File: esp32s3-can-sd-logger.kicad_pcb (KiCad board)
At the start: 4 copper layers, 84 x 100 mm, 194 parts, among them J1 PWR + CAN harness, J10 Sensor harness, J2 USB-C, J3 UART0, J4 I2C / Qwiic, J5 SPI, J6 WS2812, J7 Spare IO, J8 Rail break-out, J9 microSD push-pull, Q1 100V 6.8mOhm N-ch, Q2 P-ch 30V 3A, Q3 N-ch 60V 200mA, Q4 -20V 2.3A P-ch, Q5 60V 300mA N-ch, SW1 RESET, SW2 BOOT, U1 LM74700-Q1, U2 TLV431A, U3 LM5164 (5V), U4 LM5164 (3V3), U5 ESP32-S3-WROOM-1-N16R8, U6 USBLC6-2SC6, U7 74AHCT1G125, U8 TJA1051T/3, U9 ADS1115

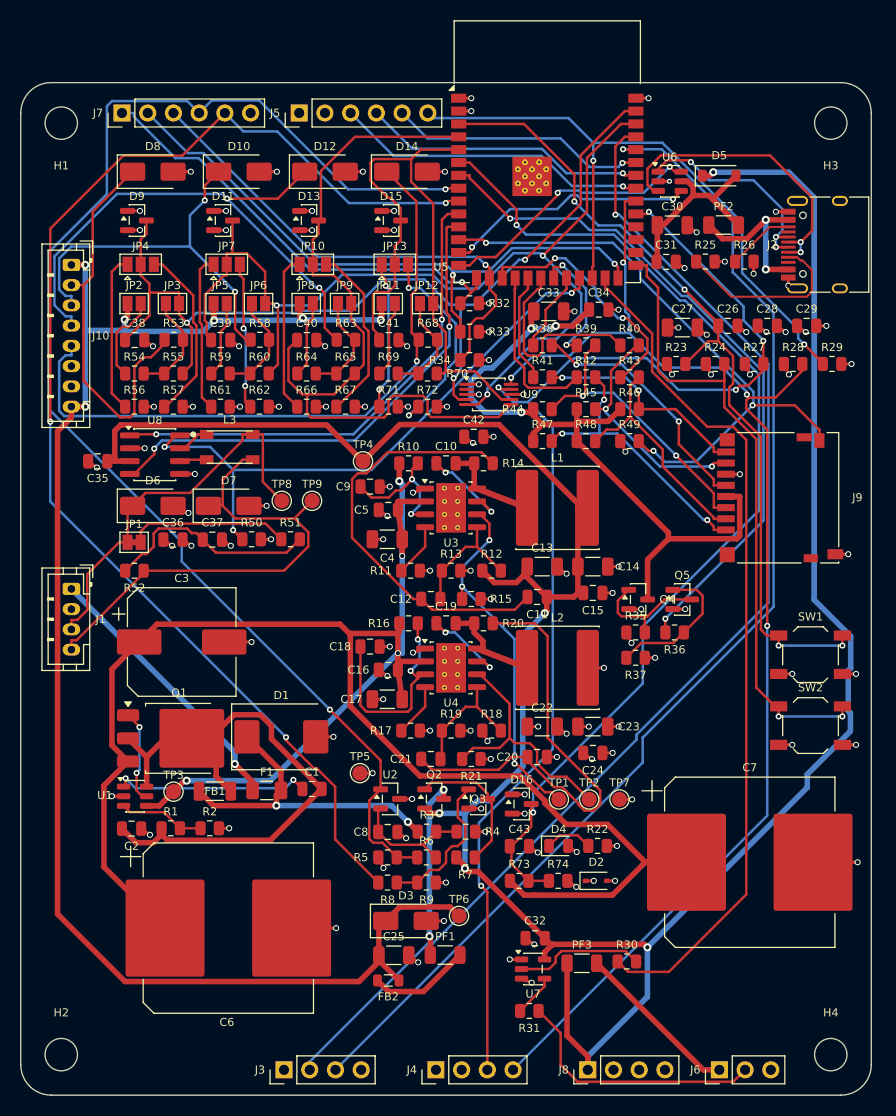
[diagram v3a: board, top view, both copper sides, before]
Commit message: USB OVP, card-slot ESD, SD test points, and a gold-standard schematic
Hardware, all simulation- or review-driven:
- USB overvoltage cutoff: TLV431 + AO3401 + MMBT3906 series switch on
  VBUS, tripping at 5.77 V. Re-simulated: a compliant 5 V source passes
  at 4.99 V, the switch opens at 5.95 V of brick, and the +5V rail never
  exceeds 5.2 V from anything up to 14 V -- where a 9 V brick previously
  drove it to 8.4 V against the TJA1051's 6 V absolute maximum.
  Off-the-shelf OVP parts were rejected first: the TPS25200 class cuts
  off near 7 V, which is no protection for a 6 V limit.
- Two SRV05-4 arrays clamp every microSD card contact (LCSC C13612);
  until now the ESP32's ~2 kV pin diodes were all that stood behind a
  card swapped by hand after every session.
- A second USBLC6 clamps the USB-C CC pins -- the first contacts every
  plug insertion touches, previously landing on bare 5.1k resistors.
- Test points on SD_CLK and SD_CMD, the most likely scope targets at
  bring-up and otherwise reachable only on fine-pitch pads.

The schematic itself was rebuilt to read like a reference design
(RejsaCAN was the benchmark): every circuit is now a hand-drawn block --
power-fail detector, sensor-rail switch, USB OVP, connector pull-
resistor clusters, and a single utility panel for test points, ERC
flags, mounting holes and the power LED. Sentence-length values became
part numbers ("0.2A PTC", "AO3401A", "600R") with ratings kept in
hidden fields, which also answers the external review's value-hygiene
findings. Title blocks carry rev B and a date. The Power sheet shrank
from A2 back to A3 in the process.

gen/README.md now documents the whole pipeline -- stages, the block-
drawing conventions with per-rotation pin geometry, the junction rules,
and the traps (property newlines, off-grid points, anchors keeping
their natural rotation) -- so the next board reuses all of it.

Board: 84 x 100, 0 DRC violations, 0 unconnected, 0 courtyard overlaps,
physical audit clean. BOM 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
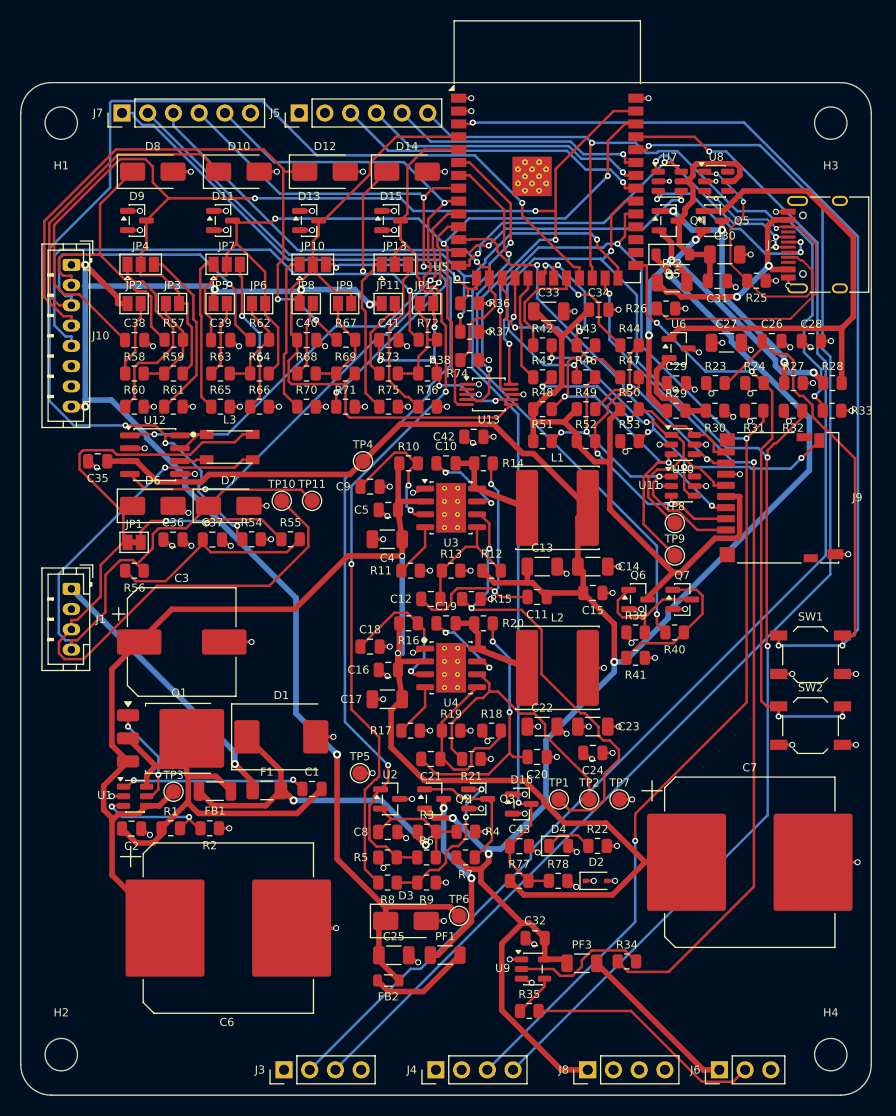
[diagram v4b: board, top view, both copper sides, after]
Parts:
- added Q6: DMG2301L, SOT-23, F.Cu at (61.0, 51.0)
- added Q7: 2N7002, SOT-23, F.Cu at (65.3, 51.0)
- added R75: 15k, R_0805_2012Metric, F.Cu at (36.3, 32.0)
- added R76: 2.21k, R_0805_2012Metric, F.Cu at (40.2, 32.0)
- added R77: 100k, R_0805_2012Metric, F.Cu at (49.2, 78.8)
- added R78: 8.2k, R_0805_2012Metric, F.Cu at (53.1, 78.8)
- added TP10: CAN_H, TestPoint_Pad_D1.5mm, F.Cu at (25.8, 41.3)
- added TP11: CAN_L, TestPoint_Pad_D1.5mm, F.Cu at (28.8, 41.3)
- added U10: SRV05-4, SOT-23-6, F.Cu at (65.4, 35.7)
- added U11: SRV05-4, SOT-23-6, F.Cu at (65.4, 39.8)
- added U12: TJA1051T/3, SOIC-8_3.9x4.9mm_P1.27mm, F.Cu at (13.2, 36.7)
- added U13: ADS1115, VSSOP-10_3x3mm_P0.5mm, F.Cu at (46.2, 30.8)
- FB1: value 600R @ 100MHz 3A -> 600R
- FB2: value 600R @ 100MHz 2A -> 600R
- L1: value 33uH 3A -> 33uH
- L2: value 22uH 3A -> 22uH
- L3: value 51uH CMC -> 51uH
- PF1: value 0.2A hold / 0.4A trip -> 0.2A PTC
- Q1: value 100V 6.8mOhm N-ch -> IPD068N10
- Q2: value P-ch 30V 3A -> AO3401A
- Q3: value N-ch 60V 200mA -> 2N7002
- Q4: value -20V 2.3A P-ch -> AO3401A
- Q5: value 60V 300mA N-ch -> MMBT3906
- R27: value 4.7k -> 100k
- R28: value 4.7k -> 10k
- R29: value 10k -> 100k
- R30: value 33 -> 27.4k
- R31: value 100 -> 4.7k
- R32: value 10k -> 4.7k
- R34, R44, R45, R46, R47: value 10k -> 33
- R35: value 100k -> 100
- R36: value 1k -> 10k
- R37: value 100k -> 10k
- R38: value 33 -> 10k
- R39, R41: value 33 -> 100k
- R40: value 33 -> 1k
- R49: value 47k -> 10k
- R51, R52: value 60.4 -> 10k
- R53: value 1k -> 47k
- R54, R59, R64, R69: value 2.49k -> 10k
- R55: value 10k -> 60.4
- R56: value 15k -> 60.4
- R57, R62, R67, R72: value 2.21k -> 1k
- R58, R63, R68: value 1k -> 2.49k
- R60, R65, R70: value 10k -> 15k
- R61, R66, R71: value 15k -> 2.21k
- R73: value 100k -> 2.49k
- R74: value 8.2k -> 10k
- TP8: value CAN_H -> SD_CLK
- TP9: value CAN_L -> SD_CMD
- U6: value USBLC6-2SC6 -> TLV431A; footprint SOT-23-6 -> SOT-23
- U7: value 74AHCT1G125 -> USBLC6-2SC6; footprint SOT-23-5 -> SOT-23-6
- U8: value TJA1051T/3 -> USBLC6-2SC6; footprint SOIC-8_3.9x4.9mm_P1.27mm -> SOT-23-6
- U9: value ADS1115 -> 74AHCT1G125; footprint VSSOP-10_3x3mm_P0.5mm -> SOT-23-5
- moved U7 79.0 mm to (64.1, 9.74)
- moved R31 63.3 mm to (72.4, 32.4)
- moved U8 61.7 mm to (68.7, 9.74)
- moved R34 61.4 mm to (59.9, 86.8)
- moved U9 56.9 mm to (50.6, 87.5)
- moved R30 55.1 mm to (68.6, 32.4)
- moved R73 51.7 mm to (36.3, 28.7)
- moved R74 51.7 mm to (40.2, 28.7)
- moved R52 46.4 mm to (55.8, 35.4)
- moved R53 46.1 mm to (60.1, 35.4)
- moved R50 39.5 mm to (60.1, 32.3)
- moved TP8 38.9 mm to (64.6, 43.5)
- moved R35 38.8 mm to (50.2, 91.7)
- moved R36 38.3 mm to (44.3, 21.8)
- moved Q4 37.5 mm to (64.0, 13.6)
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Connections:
- PF2 pad 2: VBUS -> VBUS_R
- Q4 pad 1: SD_PG -> VBUS_G
- Q4 pad 2: +3V3 -> VBUS_R
- Q4 pad 3: SD_VDD -> VBUS
- Q5 pad 1: SD_EN_G -> VBUS_OV
- Q5 pad 2: GND -> VBUS_R
- Q5 pad 3: SD_PG -> VBUS_G
- R27 pad 1: +3V3 -> VBUS_G
- R27 pad 2: I2C_SDA -> GND
- R28 pad 1: +3V3 -> VBUS_R
- R28 pad 2: I2C_SCL -> VBUS_OV
- R29 pad 1: SPI_CS -> VBUS_R
- R29 pad 2: +3V3 -> VBUS_OVS
- R30 pad 1: LED_DIN_MCU -> VBUS_OVS
- R30 pad 2: LED_DIN_A -> GND
- R31 pad 1: LED_DIN -> +3V3
- R31 pad 2: LED_DIN_J -> I2C_SDA
- R32 pad 1: IO3 -> +3V3
- R32 pad 2: GND -> I2C_SCL
- R33 pad 1: IO45 -> SPI_CS
- R33 pad 2: GND -> +3V3
- R34 pad 1: IO46 -> LED_DIN_MCU
- R34 pad 2: GND -> LED_DIN_A
- R35 pad 1: +3V3 -> LED_DIN
- R35 pad 2: SD_PG -> LED_DIN_J
- R36 pad 1: SD_PWR_EN -> IO3
- R36 pad 2: SD_EN_G -> GND
- R37 pad 1: SD_EN_G -> IO45
- R38 pad 1: SD_CLK -> IO46
- R38 pad 2: SD_CLK_C -> GND
- R39 pad 1: SD_CMD -> +3V3
- R39 pad 2: SD_CMD_C -> SD_PG
- R40 pad 1: SD_D0 -> SD_PWR_EN
- R40 pad 2: SD_D0_C -> SD_EN_G
- R41 pad 1: SD_D1 -> SD_EN_G
- R41 pad 2: SD_D1_C -> GND
- R42 pad 1: SD_D2 -> SD_CLK
- R42 pad 2: SD_D2_C -> SD_CLK_C
- R43 pad 1: SD_D3 -> SD_CMD
- R43 pad 2: SD_D3_C -> SD_CMD_C
- R44 pad 1: SD_VDD -> SD_D0
- R44 pad 2: SD_CMD_C -> SD_D0_C
- R45 pad 1: SD_VDD -> SD_D1
- R45 pad 2: SD_D0_C -> SD_D1_C
- R46 pad 1: SD_VDD -> SD_D2
- R46 pad 2: SD_D1_C -> SD_D2_C
- R47 pad 1: SD_VDD -> SD_D3
- R47 pad 2: SD_D2_C -> SD_D3_C
- R48 pad 2: SD_D3_C -> SD_CMD_C
- R49 pad 1: +3V3 -> SD_VDD
- R49 pad 2: SD_CD -> SD_D0_C
- R50 pad 1: CAN_S -> SD_VDD
- R50 pad 2: GND -> SD_D1_C
- R51 pad 1: TERM_A -> SD_VDD
- R51 pad 2: CAN_SPLIT -> SD_D2_C
- R52 pad 1: CAN_SPLIT -> SD_VDD
- R52 pad 2: CAN_L -> SD_D3_C
- R53 pad 1: AIN1_IN -> +3V3
- R53 pad 2: AIN1_A -> SD_CD
- R54 pad 1: AIN1_PU -> CAN_S
- R54 pad 2: AIN1_A -> GND
- R55 pad 1: AIN1_A -> TERM_A
- R55 pad 2: AIN1 -> CAN_SPLIT
- R56 pad 1: AIN1_R1 -> CAN_SPLIT
- R56 pad 2: GND -> CAN_L
- R57 pad 1: AIN1_R2 -> AIN1_IN
- R57 pad 2: GND -> AIN1_A
- R58 pad 1: AIN2_IN -> AIN1_PU
- R58 pad 2: AIN2_A -> AIN1_A
- R59 pad 1: AIN2_PU -> AIN1_A
- R59 pad 2: AIN2_A -> AIN1
- R60 pad 1: AIN2_A -> AIN1_R1
- R60 pad 2: AIN2 -> GND
- R61 pad 1: AIN2_R1 -> AIN1_R2
- R62 pad 1: AIN2_R2 -> AIN2_IN
- R62 pad 2: GND -> AIN2_A
- R63 pad 1: AIN3_IN -> AIN2_PU
- R63 pad 2: AIN3_A -> AIN2_A
- R64 pad 1: AIN3_PU -> AIN2_A
- R64 pad 2: AIN3_A -> AIN2
- R65 pad 1: AIN3_A -> AIN2_R1
- R65 pad 2: AIN3 -> GND
- R66 pad 1: AIN3_R1 -> AIN2_R2
- R67 pad 1: AIN3_R2 -> AIN3_IN
- R67 pad 2: GND -> AIN3_A
- R68 pad 1: AIN4_IN -> AIN3_PU
- R68 pad 2: AIN4_A -> AIN3_A
- R69 pad 1: AIN4_PU -> AIN3_A
- R69 pad 2: AIN4_A -> AIN3
- R70 pad 1: AIN4_A -> AIN3_R1
- R70 pad 2: AIN4 -> GND
- R71 pad 1: AIN4_R1 -> AIN3_R2
- R72 pad 1: AIN4_R2 -> AIN4_IN
- R72 pad 2: GND -> AIN4_A
- R73 pad 1: +VBAT -> AIN4_PU
- R73 pad 2: VBAT_SNS -> AIN4_A
- R74 pad 1: VBAT_SNS -> AIN4_A
- R74 pad 2: GND -> AIN4
- TP8 pad 1: CAN_H -> SD_CLK_C
- TP9 pad 1: CAN_L -> SD_CMD_C
- U6 pad 1: USB_DP_CON -> VBUS_OV
- U6 pad 2: GND -> VBUS_OVS
- U6 pad 3: USB_DM_CON -> GND
- U7 pad 1: GND -> USB_DP_CON
- U7 pad 2: LED_DIN_A -> GND
- U7 pad 3: GND -> USB_DM_CON
- U7 pad 4: LED_DIN -> USB_DM
- U7 pad 5: +5V -> VBUS
- U8 pad 1: CAN_TX -> USB_CC1
- U8 pad 3: +5V -> USB_CC2
- U8 pad 4: CAN_RX -> (no net)
- U8 pad 5: +3V3 -> VBUS
- U8 pad 6: CANL_T -> (no net)
- U9 pad 2: (no net) -> LED_DIN_A
- U9 pad 4: AIN1 -> LED_DIN
- U9 pad 5: AIN2 -> +5V
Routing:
- net CAN_S: track 59.7 -> 115.6 mm, vias 3 -> 4
- net MCU_EN: track 82.1 -> 134.1 mm, vias 4 -> 3
- net +5V: track 261.6 -> 211.4 mm, vias 5 -> 4
- net VBUS_OV: track 0.00 -> 49.9 mm
- net VBUS_R: track 0.00 -> 47.5 mm, vias 0 -> 4
- net CAN_H: track 39.0 -> 79.5 mm
- net AIN1: track 93.7 -> 132.2 mm, vias 3 -> 4
- net +VBAT: track 191.9 -> 158.1 mm, vias 4 -> 2
- net USB_CC2: track 6.67 -> 35.3 mm, vias 0 -> 2
- net PWR_FAIL: track 134.0 -> 107.2 mm, vias 2 -> 3
- net VBUS_G: track 0.00 -> 25.6 mm, vias 0 -> 3
- net SENS_EN: track 127.0 -> 102.6 mm
- net VBAT_SNS: track 103.2 -> 82.0 mm
- net AIN2_IN: track 39.4 -> 60.0 mm, vias 2 -> 1
- net RAMP_3V3: track 46.1 -> 25.7 mm, vias 0 -> 2
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
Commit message: Studies 9-11, post-route extraction, strap audit, readable labels, production BOM numbers
New tests, run against the final board:
- audit_routes.py: Dijkstra IR drop over the routed copper (worst 55 mV
  at rated current), SD/USB/CAN routed lengths (USB pair matched to
  1.1 mm), buck switch-node copper area. All clean.
- audit_straps.py: every ESP32-S3 strapping pin against what the netlist
  hangs on it; all five boot in their required state.
- simulate.py 9, stability: the LM5164 ripple-injection criterion across
  the input window. Found the ramp thin (10.6 mV) at a legitimate 8 V
  operating point -- ramp caps changed 3.3 nF -> 2.2 nF, now 15.8 mV+
  everywhere above crank voltages. Board rebuilt: 0 DRC, 0 unconnected,
  0 overlaps.
- simulate.py 10, CAN bus: TJA1051 through the choke and split
  termination into 5 m of terminated line -- 2.00 V dominant at the far
  end, no overshoot.
- simulate.py 11, budgets: enclosure thermal for the in-dash mount
  (sealed ABS is fine in the dash, would exceed the electrolytics' 105 C
  in an engine bay -- documented), fuse derating 69 %, I2C rise time vs
  Qwiic chains, WS2812 count, SD switch drop, connector contacts.
- tolerance MC gains the ride-through corner: 36 ms at caps -20 % /
  load +40 %, still covering a healthy-card flush.

Schematic readability, second pass: net-name labels moved onto short
vertical spurs clear of the circuits (deleting them outright renames
nets to Net-(R5-Pad2) and breaks name-based verification -- now in
gen/README.md), end-labels extend away from what they feed, and the
sensor-switch block redrawn at 1.5x pitch. Reversed-5V behaviour per
connector documented in the README.

BOM production pass: verified LCSC numbers added for the TVS families,
BAT54S, MM3Z zener and 2N7002s (21 numbered lines); the 39 blank lines
are JLC-auto-matched basic R/C; the 12 extended lines that must be
hand-matched in the order UI are listed in README 11. No guessed part
numbers.

gen/README.md gains the readab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
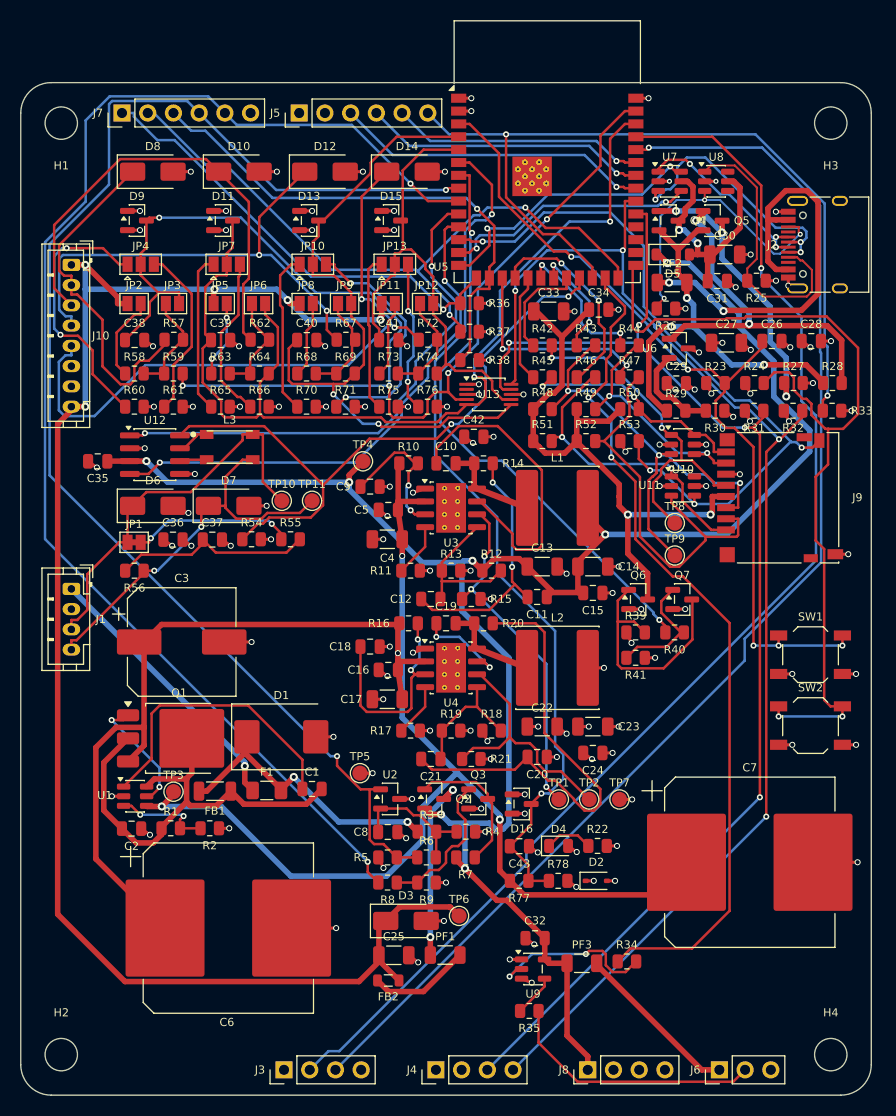
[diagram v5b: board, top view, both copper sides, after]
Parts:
- C11, C20: value 3.3nF -> 2.2nF
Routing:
- net CAN_S: track 115.6 -> 65.4 mm, vias 4 -> 2
- net MCU_EN: track 134.1 -> 84.6 mm, vias 3 -> 5
- net CAN_H: track 79.5 -> 39.0 mm
- net SENS_EN: track 102.6 -> 132.7 mm, vias 3 -> 2
- net CAN_L: track 67.7 -> 38.8 mm, vias 1 -> 2
- net +VBAT: track 158.1 -> 185.9 mm, vias 2 -> 4
- net PWR_FAIL: track 107.2 -> 134.0 mm, vias 3 -> 2
- net MCU_BOOT: track 62.7 -> 89.2 mm, vias 4 -> 2
- net +5V: track 211.4 -> 187.9 mm, vias 4 -> 7
- net +5VS: track 135.9 -> 159.1 mm, vias 6 -> 5
- net BST_5V: track 8.52 -> 31.3 mm, vias 2 -> 0
- net VBUS_IN: track 21.2 -> 42.5 mm
- net RAMP_3V3: track 25.7 -> 46.0 mm, vias 2 -> 0
- net SD_CD: track 55.2 -> 72.5 mm
- net SD_D3_C: track 26.3 -> 40.3 mm, vias 2 -> 0
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
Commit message: Board change: termination off by default, 0-5 V sensors by default, 2x330 uF
Three defaults changed in gen/generate_schematic.py, then the whole chain
regenerated: schematic, board, fab, plots. Schematic is ERC-clean at 206
components / 114 nets; the board rebuilt to 0 DRC violations and 0
unconnected; fab BOM and CPL agree at 178 designators.

CAN termination now ships OFF. JP1 moves from SolderJumper-2_Bridged to
_Open. The board was shipping terminated, matching the Autosport Labs
convention, but the common case here is plugging into a vehicle bus that
is already terminated at both ends — where a third 120 ohm takes the pair
to about 40 ohm and can stop the bus working. Defaulting on made that an
easy mistake; defaulting off means there is nothing to remember before
plugging into a car, and bridging JP1 is a deliberate act for a bench bus
where this board is an end node.

Analog channels now ship in the 0-5 V range. The four RANGE jumpers move
from SolderJumper-3_Open to _Bridged12, closing the 15k leg. They were
shipping fully open, which is no divider at all, so a 5 V sensor needed a
jumper somebody had to remember to fit — and the firmware's DIVIDER_GAIN
of 1.7334 assumed the 0-5 V ratio, so an unfitted jumper read 73 % high.
Board and firmware defaults now agree out of the box.

Ride-through bank 540 -> 760 uF. C6/C7 go 220 -> 330 uF in CP_Elec_16x22.
That footprint is identical to the 16x17.5 it replaces in every copper,
courtyard, silk and fab layer — only the 3D can is 4.5 mm taller — so the
extra 220 uF costs nothing but enclosure height, and the routed board did
not have to move for it.

It is not free everywhere: inrush I2t is linear in C, so the 2 A fuse's
margin drops from ~5x to ~3.6x. Noted in the generator next to the value
so the next person to grow the bank sees it.

ngspice is not installed here, so the new hold-up figures (152 / 75 ms,
from 108 / 53) are SCALED, not measured — hold-up is linear in C for a
constant-power load over a fixed window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
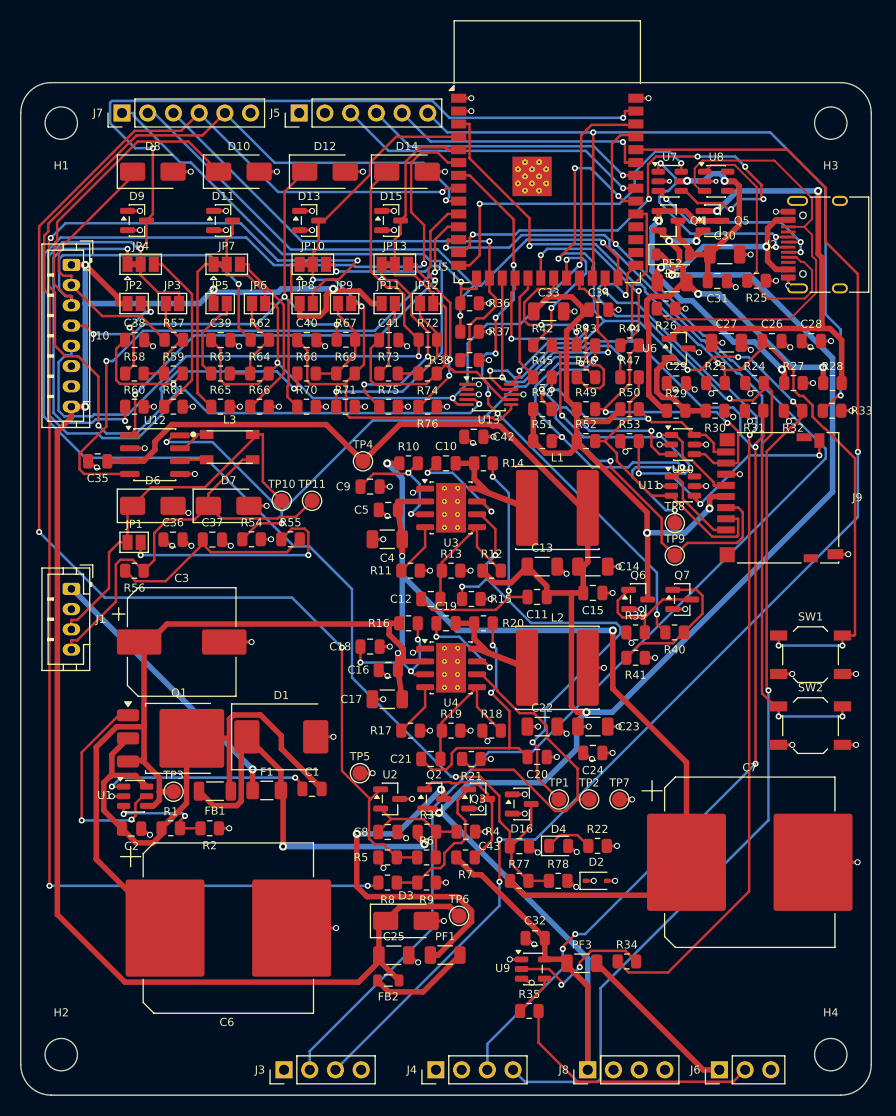
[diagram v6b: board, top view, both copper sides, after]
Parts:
- C6, C7: value 220uF -> 330uF; footprint CP_Elec_16x17.5 -> CP_Elec_16x22
- JP1: value TERM (default ON) -> TERM (default OFF); footprint SolderJumper-2_P1.3mm_Bridged_Pad1.0x1.5mm -> SolderJumper-2_P1.3mm_Open_Pad1.0x1.5mm
- JP10: value RANGE3 -> RANGE3 (default 0-5V); footprint SolderJumper-3_P1.3mm_Open_Pad1.0x1.5mm -> SolderJumper-3_P1.3mm_Bridged12_Pad1.0x1.5mm
- JP13: value RANGE4 -> RANGE4 (default 0-5V); footprint SolderJumper-3_P1.3mm_Open_Pad1.0x1.5mm -> SolderJumper-3_P1.3mm_Bridged12_Pad1.0x1.5mm
- JP4: value RANGE1 -> RANGE1 (default 0-5V); footprint SolderJumper-3_P1.3mm_Open_Pad1.0x1.5mm -> SolderJumper-3_P1.3mm_Bridged12_Pad1.0x1.5mm
- JP7: value RANGE2 -> RANGE2 (default 0-5V); footprint SolderJumper-3_P1.3mm_Open_Pad1.0x1.5mm -> SolderJumper-3_P1.3mm_Bridged12_Pad1.0x1.5mm
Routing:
- net AIN3_PU: track 7.54 -> 86.4 mm, vias 0 -> 4
- net VBAT_SNS: track 86.5 -> 153.9 mm
- net +5V: track 187.9 -> 241.0 mm, vias 7 -> 3
- net AIN1: track 123.8 -> 165.7 mm
- net USB_DM: track 25.2 -> 46.9 mm, vias 2 -> 6
- net VBUS_IN: track 42.5 -> 21.0 mm
- net BST_5V: track 31.3 -> 11.0 mm, vias 0 -> 2
- net RAMP_3V3: track 46.0 -> 26.2 mm, vias 0 -> 2
- net MCU_BOOT: track 89.2 -> 71.2 mm, vias 2 -> 4
- net VSENS_SW: track 18.5 -> 35.2 mm
- net I2C_SCL: track 131.0 -> 147.4 mm, vias 4 -> 8
- net USB_CC2: track 29.8 -> 45.3 mm, vias 3 -> 0
- net SENS_EN: track 132.7 -> 148.2 mm, vias 2 -> 3
- net PG_5V: track 34.5 -> 48.5 mm
- net AIN2_IN: track 46.5 -> 60.3 mm, vias 0 -> 1
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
